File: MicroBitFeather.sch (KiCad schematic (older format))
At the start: 16 parts, among them J1 Feather_Long, J2 Barrel_Jack_MountingPin, J3 Feather_Short, J4 NeoPixels, J5 microbit_edge_connector, U1 74AHCT125, U2 MCP1702-3302E_TO92

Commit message: I meant for NeoPixel pin to be P0.
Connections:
- net P0: now also U1.2 (1A)
- net P1: no longer U1.2 (1A)
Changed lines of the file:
@@
 Connection ~ 4200 5300
 Text Label 4000 4300 0    50   ~ 0
-P1
+P0
 Wire Wire Line
 	4000 4300 4300 4300

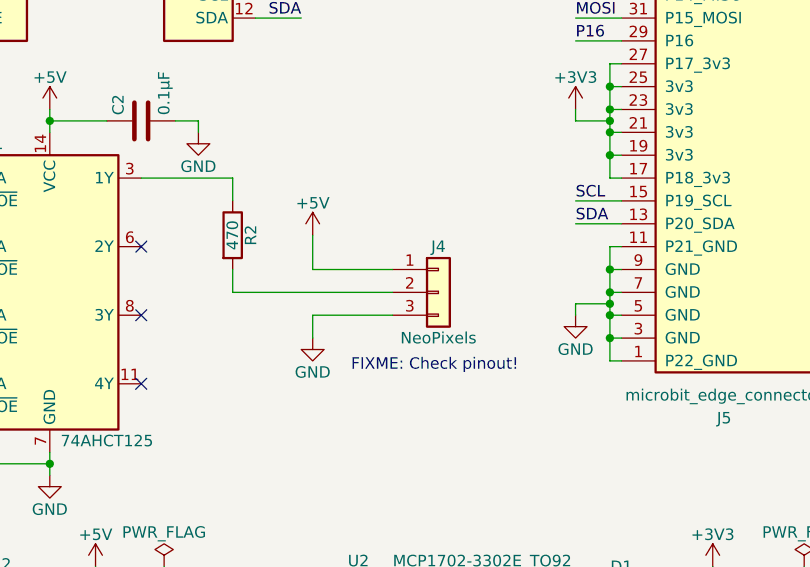
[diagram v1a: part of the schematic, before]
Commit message: I had the pinout for the NeoPixel connector wrong.
https://cdn.sparkfun.com/datasheets/Prototyping/ACCA-1495.pdf
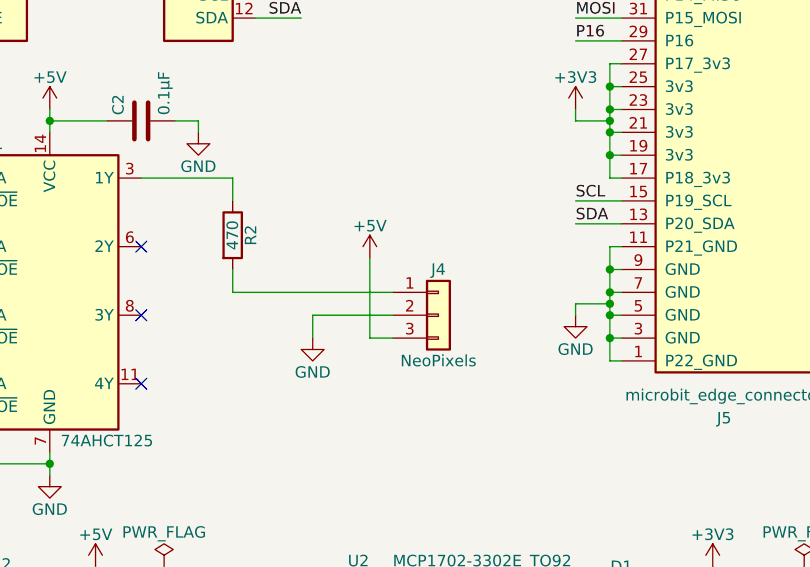
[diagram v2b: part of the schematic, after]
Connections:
- net +5V: now also J4.3 (Pin_3); no longer J4.1 (Pin_1)
- net GND: now also J4.2 (Pin_2); no longer J4.3 (Pin_3)
- net at R2.2: now also J4.1 (Pin_1); no longer J4.2 (Pin_2)
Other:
- note removed: "FIXME: Check pinout!"
- moved on the sheet: J4
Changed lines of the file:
@@
 Sheet 1 1
 Title "Neopixel and FeatherWing adapter for Micro:Bit"
-Date "2017-08-30"
+Date "2017-08-31"
 Rev ""
 Comp "Patrick Pelletier"
@@
 L Conn_01x03 J4
 U 1 1 5B8792D8
-P 6400 4800
-F 0 "J4" H 6400 5000 50  0000 C CNN
-F 1 "NeoPixels" H 6400 4600 50  0000 C CNN
-F 2 "Connectors_JST:JST_PH_S3B-PH-K_03x2.00mm_Angled" H 6400 4800 50  0001 C CNN
-F 3 "" H 6400 4800 50  0001 C CNN
-F 4 "S3B-PH-K-S(LF)(SN)" H 6400 4800 60  0001 C CNN "MPN"
-F 5 "CONN HEADER PH SIDE 3POS 2MM" H 6400 4800 60  0001 C CNN "Description"
-F 6 "455-1720-ND" H 6400 4800 60  0001 C CNN "Digi-Key_PN"
-	1    6400 4800
-	1    0    0    -1
-$EndComp
-Text Notes 6750 5150 2    50   ~ 0
-FIXME: Check pinout!
+P 6400 4900
+F 0 "J4" H 6400 5100 50  0000 C CNN
+F 1 "NeoPixels" H 6400 4700 50  0000 C CNN
+F 2 "Connectors_JST:JST_PH_S3B-PH-K_03x2.00mm_Angled" H 6400 4900 50  0001 C CNN
+F 3 "" H 6400 4900 50  0001 C CNN
+F 4 "S3B-PH-K-S(LF)(SN)" H 6400 4900 60  0001 C CNN "MPN"
+F 5 "CONN HEADER PH SIDE 3POS 2MM" H 6400 4900 60  0001 C CNN "Description"
+F 6 "455-1720-ND" H 6400 4900 60  0001 C CNN "Digi-Key_PN"
+	1    6400 4900
+	1    0    0    -1
+$EndComp
 $Comp
 L GND #PWR07
@@
 L +5V #PWR08
 U 1 1 5B8794C4
-P 5850 4550
-F 0 "#PWR08" H 5850 4400 50  0001 C CNN
-F 1 "+5V" H 5850 4690 50  0000 C CNN
-F 2 "" H 5850 4550 50  0001 C CNN
-F 3 "" H 5850 4550 50  0001 C CNN
-	1    5850 4550
-	1    0    0    -1
-$EndComp
-Wire Wire Line
-	5850 4550 5850 4700
-Wire Wire Line
-	5850 4700 6200 4700
+P 6100 4650
+F 0 "#PWR08" H 6100 4500 50  0001 C CNN
+F 1 "+5V" H 6100 4790 50  0000 C CNN
+F 2 "" H 6100 4650 50  0001 C CNN
+F 3 "" H 6100 4650 50  0001 C CNN
+	1    6100 4650
+	1    0    0    -1
+$EndComp
 Wire Wire Line
 	5850 5000 5850 4900
@@
 Text Notes 3800 6350 0    60   ~ 0
 Check\nconnector\ndiameter!
+Wire Wire Line
+	6100 4650 6100 5000
+Wire Wire Line
+	6100 5000 6200 5000
 $EndSCHEMATC
